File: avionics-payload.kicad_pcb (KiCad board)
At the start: 2 copper layers, 80 x 80 mm, 25 parts, among them J1 Conn_Coaxial_x2, SW1 SW_Push, SW2 SW_Push, U1 ADXL357BEZ, U2 Teensy4.0, U3 RFM96W-433S2, U4 ublox_SAM-M8Q, U5 MS5607-02BA

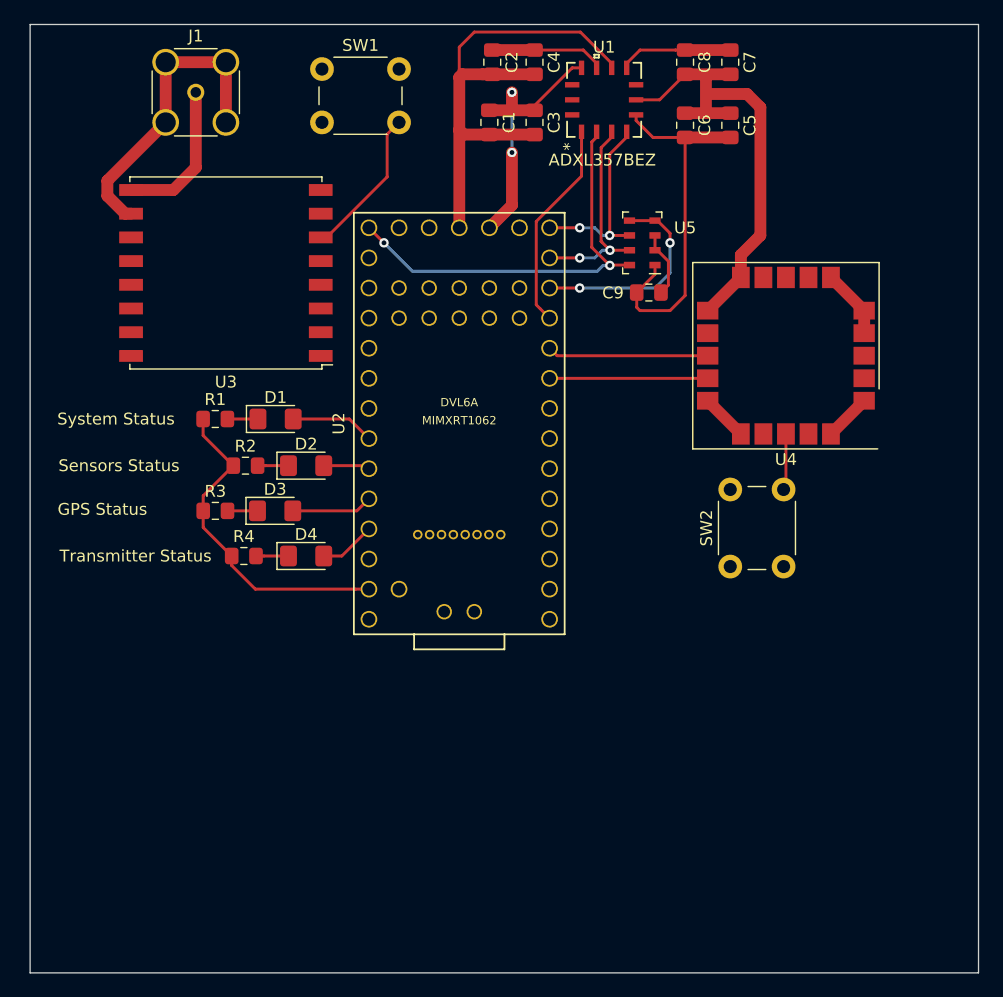
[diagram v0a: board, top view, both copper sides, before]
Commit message: Added power module and made schematic more modular.
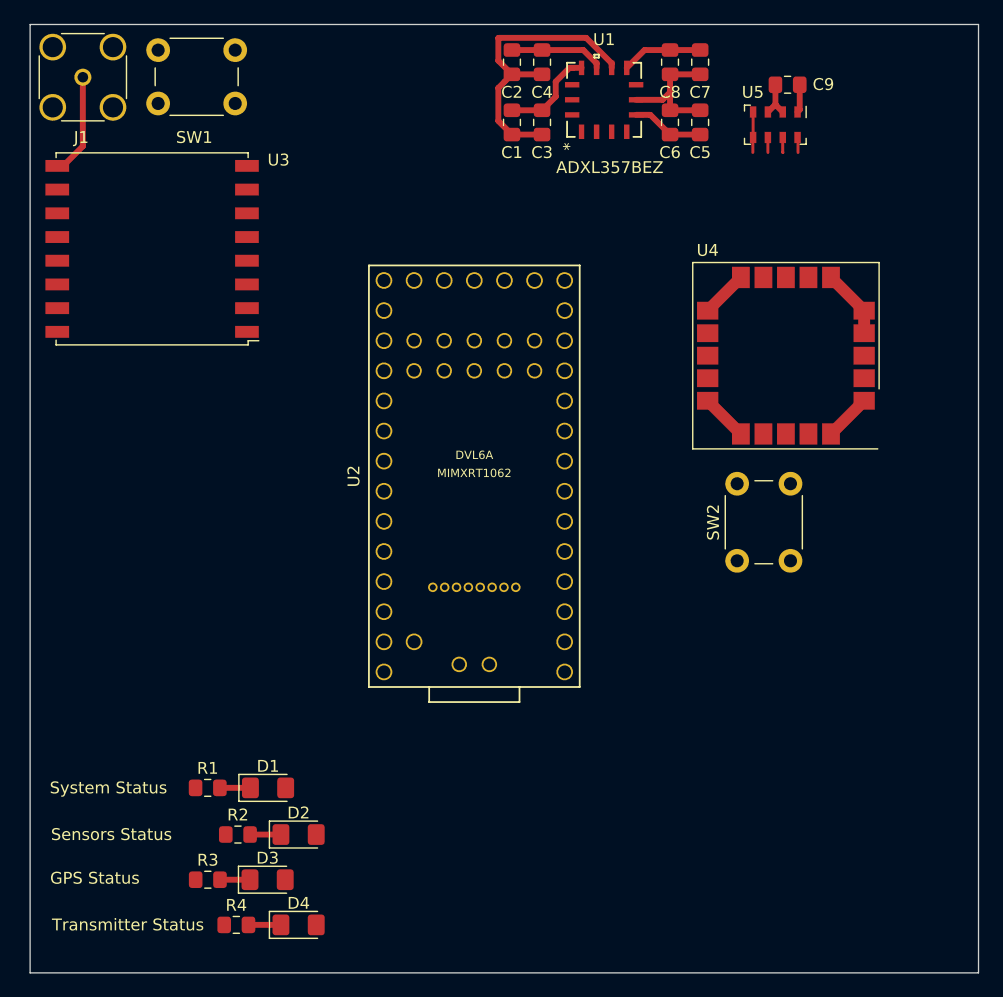
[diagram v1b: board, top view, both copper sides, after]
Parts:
- moved D1 31.1 mm to (60.1, 104.4)
- moved D2 31.1 mm to (62.6, 108.3)
- moved D3 31.1 mm to (60.0, 112.1)
- moved R1 31.1 mm to (55.0, 104.4)
- moved R2 31.1 mm to (57.5, 108.3)
- moved R3 31.1 mm to (55.0, 112.1)
- moved D4 31.1 mm to (62.6, 116.0)
- moved R4 31.1 mm to (57.4, 116.0)
- moved C9 21.1 mm to (103.9, 45.1), turned to 180 degrees
- moved U5 15.0 mm to (102.9, 48.5), turned to 270 degrees
- moved SW1 13.9 mm to (50.8, 42.2)
- moved J1 9.61 mm to (44.5, 44.5)
- moved U3 6.55 mm to (50.3, 58.9)
- moved U2 4.62 mm to (77.5, 78.1)
- moved C5 2.55 mm to (96.5, 48.3)
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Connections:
- J1 pad 1: Net-(J1-Pad2) -> Net-(AE1-Pad1)
- J1 pad 2: GND -> Net-(J1-Pad2)
- U2 pad 35: (no net) -> Net-(U2-Pad35)
- U2 pad 36: (no net) -> Net-(U2-Pad36)
- U2 pad 37: (no net) -> Net-(U2-Pad37)
- U2 pad 38: (no net) -> Net-(U2-Pad38)
- U2 pad 39: (no net) -> Net-(U2-Pad39)
- U2 pad 40: (no net) -> Net-(U2-Pad40)
- U2 pad 41: (no net) -> Net-(U2-Pad41)
- U2 pad 42: (no net) -> Net-(U2-Pad42)
- U2 pad 43: (no net) -> Net-(U2-Pad43)
- U2 pad 44: (no net) -> Net-(U2-Pad44)
- U2 pad 45: (no net) -> MISO2
- U2 pad 46: (no net) -> MOSI2
- U2 pad 47: (no net) -> GND
- U2 pad 48: (no net) -> CS2
- U2 pad 49: SCK2 -> +3V3
- U2 pad 50: CS2 -> SCK2
- U2 pad 51: MOSI2 -> Net-(U2-Pad51)
- U2 pad 52: MISO2 -> Net-(U2-Pad52)
- U2 pad 53: (no net) -> Net-(U2-Pad53)
- U2 pad 54: (no net) -> Net-(U2-Pad54)
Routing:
- net GND: track 180.8 -> 57.9 mm
- net +3V3: track 58.8 -> 16.6 mm, vias 2 -> 0
- net SCK1: track 35.5 -> 1.29 mm, vias 2 -> 0
- net CS1:2: track 17.8 -> 0.00 mm
- net MOSI1: track 17.3 -> 1.28 mm, vias 2 -> 0
- net MISO1: track 15.9 -> 1.27 mm, vias 2 -> 0
- net CS1:1: track 17.9 -> 3.43 mm, vias 2 -> 0
- net TX1: track 13.6 -> 0.00 mm
- net RX1: track 13.3 -> 0.01 mm
- net Net-(SW1-Pad2): track 12.7 -> 0.00 mm
- net Net-(D1-Pad2): track 7.07 -> 0.00 mm
- net Net-(D3-Pad2): track 6.84 -> 0.00 mm
- net Net-(SW2-Pad2): track 4.77 -> 0.00 mm
- net Net-(D4-Pad2): track 4.76 -> 0.00 mm
- net Net-(J1-Pad2): track 12.6 -> 8.66 mm
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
